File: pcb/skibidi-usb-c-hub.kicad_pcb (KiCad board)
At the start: 2 copper layers, 17.5 x 39 mm, 20 parts, among them U1 CH334P

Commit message: finished pcb and bom, added schematic pdf, step file for pcb, and gerbers
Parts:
- added C5: 10u, Capacitor_SMD:C_0603_1608Metric, F.Cu at (43.8, 68.8)
- added C6: 10u, Capacitor_SMD:C_0603_1608Metric, F.Cu at (42.0, 49.5)
- added C7: 10u, Capacitor_SMD:C_0603_1608Metric, F.Cu at (32.0, 68.8)
- added C8: 10u, Capacitor_SMD:C_0603_1608Metric, F.Cu at (38.8, 45.0)
- added C9: 220u, Capacitor_SMD:CP_Elec_6.3x5.8, F.Cu at (32.2, 53.0)
- C2: value 100n -> 4.7u
- TP1: footprint TestPoint:TestPoint_Pad_D1.0mm -> TestPoint:TestPoint_Pad_D2.5mm; moved to B.Cu
- moved R8 118.2 mm to (31.9, 37.0)
- moved R7 117.8 mm to (31.9, 35.5)
- moved R6 113.5 mm to (35.5, 68.8)
- moved R5 110.6 mm to (38.8, 65.8)
- moved F1 104.2 mm to (35.8, 36.9)
- moved FB1 101.5 mm to (38.2, 40.0), turned to -90 degrees
- moved D1 100.6 mm to (41.0, 36.9)
- moved R4 99.4 mm to (44.5, 55.5)
- moved R3 97.4 mm to (44.5, 57.0)
- moved TP1 95.5 mm to (45.5, 41.5)
- moved R2 85.0 mm to (44.5, 50.5)
- moved R1 84.5 mm to (44.5, 48.8)
- moved C1 3.74 mm to (36.3, 55.1), turned to -90 degrees
- moved C2 3.07 mm to (37.6, 55.9), turned to -135 degrees
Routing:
- net VBUS: track 0.00 -> 113.9 mm, vias 0 -> 11
- net Net-(USB2-CC2): track 0.00 -> 14.9 mm, vias 0 -> 2
- net Net-(USB3-CC1): track 0.00 -> 12.7 mm, vias 0 -> 2
- net Net-(USB5-CC2): track 0.00 -> 12.3 mm, vias 0 -> 4
- net Net-(USB3-CC2): track 0.00 -> 12.1 mm, vias 0 -> 2
- net Net-(USB5-CC1): track 0.00 -> 10.1 mm, vias 0 -> 2
- net Net-(USB2-CC1): track 0.00 -> 8.32 mm, vias 0 -> 2
- net Net-(USB4-CC1): track 0.00 -> 7.53 mm, vias 0 -> 2
- net Net-(USB4-CC2): track 0.00 -> 6.53 mm, vias 0 -> 2
- net Net-(D1-A1): track 0.00 -> 5.50 mm
- net GND: track 0.00 -> 5.38 mm, vias 0 -> 35
- net /USB C 4/D-: track 22.6 -> 25.3 mm
- net /USB C 4/D+: track 23.3 -> 25.9 mm
- net +3V3: track 0.00 -> 2.56 mm
- net Net-(USB1-VCC): track 0.00 -> 2.27 mm
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- added copper zone on B.Cu, net GND
- added copper zone on F.Cu, net GND
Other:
- board size 17.5 x 39 mm -> 17.5 x 40 mm

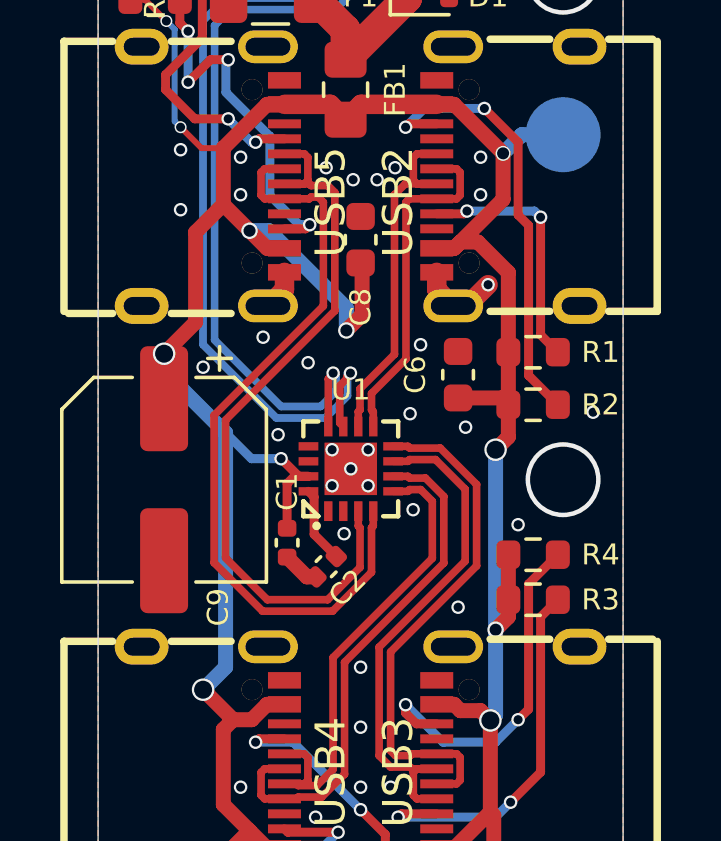
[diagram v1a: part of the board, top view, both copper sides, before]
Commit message: add cad for case
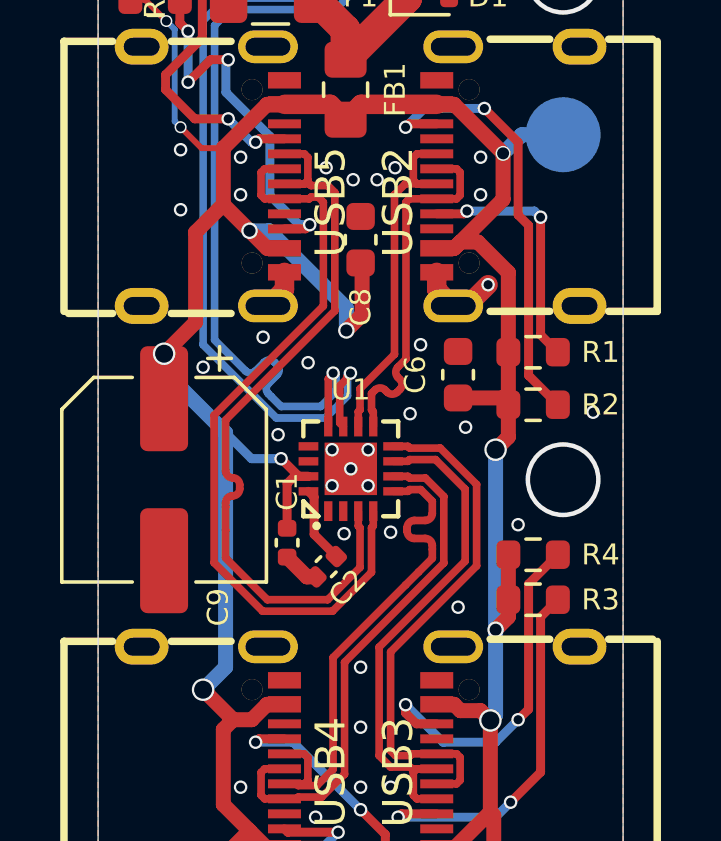
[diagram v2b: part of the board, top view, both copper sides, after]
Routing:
- net /USB A Upstream/D+: track 25.5 -> 26.8 mm
- net /USB C 3/D-: track 16.1 -> 17.3 mm
- net /USB C 1/D-: track 11.5 -> 12.2 mm
